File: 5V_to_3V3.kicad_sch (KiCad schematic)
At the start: 5 parts, among them U4 XC6206P332MR

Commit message: WIP
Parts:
- U4: footprint Package_TO_SOT_SMD:SOT-23-3 -> Package_TO_SOT_SMD:SOT-23
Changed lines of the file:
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@@
       (effects (font (size 1 1)))
     )
-    (property "Footprint" "Package_TO_SOT_SMD:SOT-23-3" (at 58.42 32.385 0)
+    (property "Footprint" "Package_TO_SOT_SMD:SOT-23" (at 58.42 32.385 0)
       (effects (font (size 1 1) italic) hide)
     )

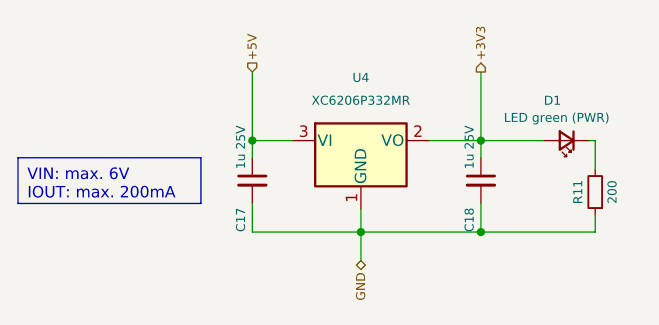
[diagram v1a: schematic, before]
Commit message: Replace 3V3 LDO for a 1A model
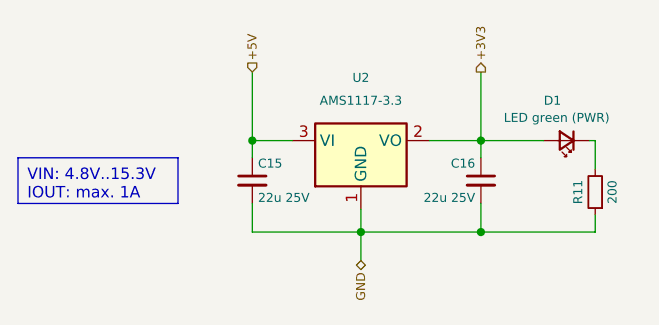
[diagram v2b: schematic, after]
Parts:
- removed C17, C18: 1u 25V, Capacitor_SMD:C_0402_1005Metric, symbol Device:C_Small
- removed U4: XC6206P332MR, Package_TO_SOT_SMD:SOT-23, symbol Regulator_Linear:XC6206PxxxMR
- added C15, C16: 22u 25V, Capacitor_SMD:C_0805_2012Metric, symbol Device:C_Small
- added U2: AMS1117-3.3, Package_TO_SOT_SMD:SOT-223-3_TabPin2, symbol Regulator_Linear:AMS1117-3.3
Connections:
- net +3V3: now also C16.1, U2.2 (VO)
- net +5V: now also C15.1, U2.3 (VI)
- net GND: now also C15.2, C16.2, U2.1 (GND)

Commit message: #2 Add silkscreen texts
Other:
- company: (none) -> easy-smart solution GmbH
- title: (none) -> STM32F4 Uno
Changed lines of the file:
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@@
 (kicad_sch (version 20230121) (generator eeschema)
   (paper "A4")
+  (title_block
+    (title "STM32F4 Uno")
+    (date "2023-10-02")
+    (rev "1.0.x-dev")
+    (company "easy-smart solution GmbH")
+  )
   (junction (at 71.755 48.26) (diameter 0) (color 0 0 0 0)
   )
